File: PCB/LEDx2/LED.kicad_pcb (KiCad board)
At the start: 2 copper layers, 70 x 70 mm, 32 parts, among them J1 Reset, J2 Wago, J3 TC2030-USB-NL-DS, J4 Wago, J5 USB-C-Socket-H, J6 Wago, J7 Wago, U6 ESP32-S3-MINI-1, U7 MD8942

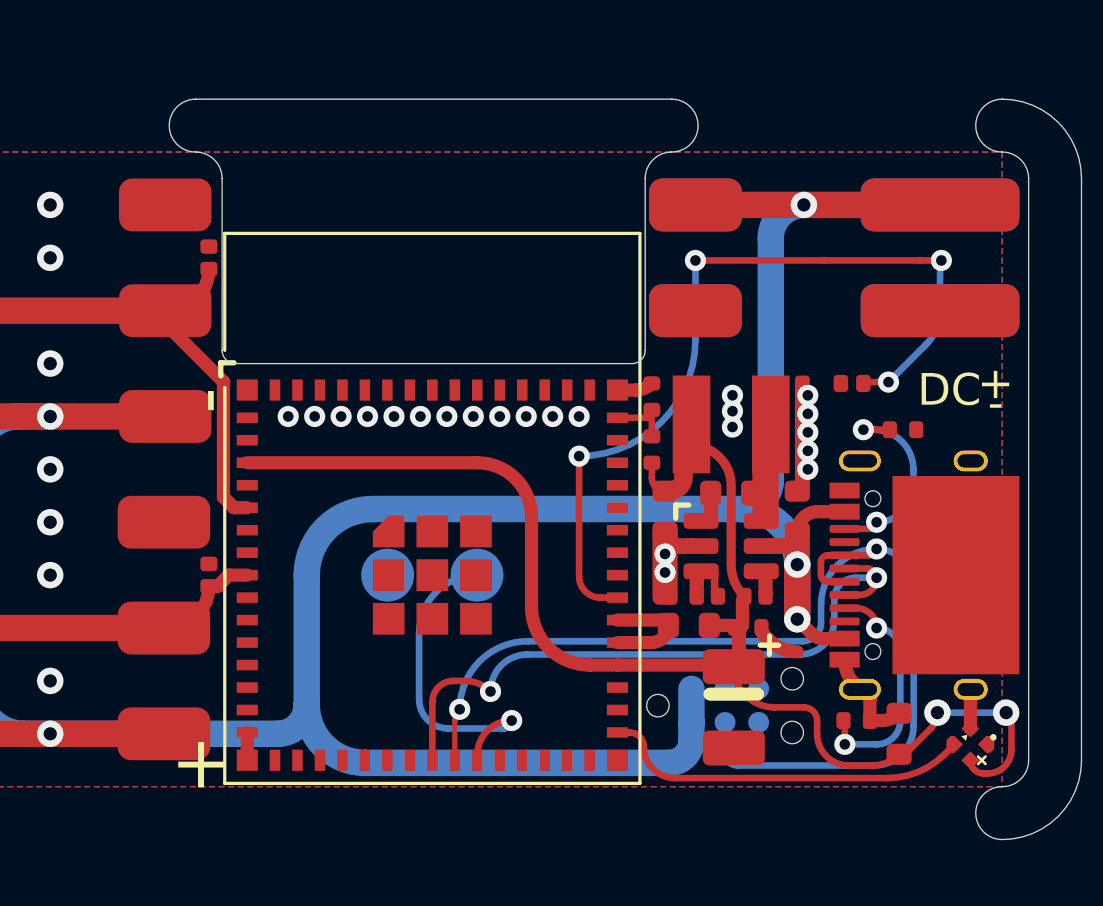
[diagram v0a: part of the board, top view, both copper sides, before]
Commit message: Tidy silkscreen
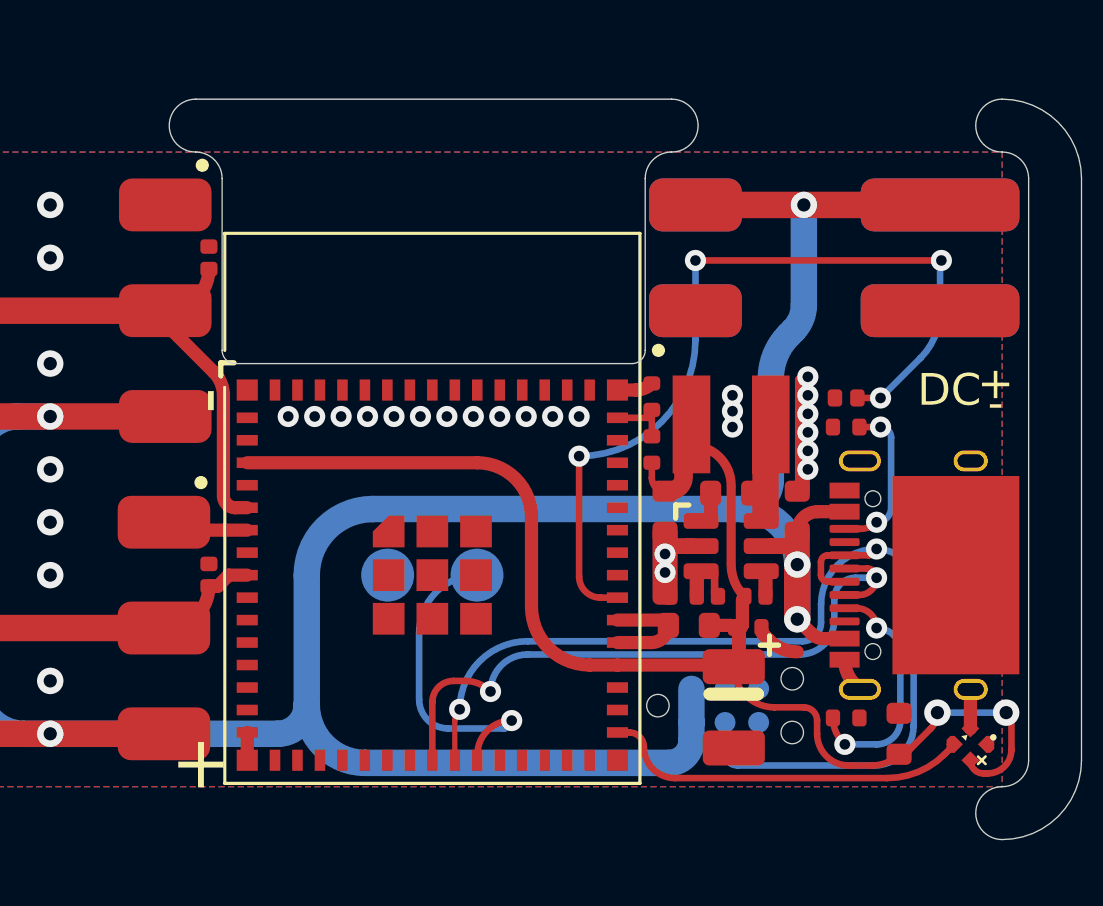
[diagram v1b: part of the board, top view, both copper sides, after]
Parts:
- moved R6 2.15 mm to (114.1, 96.4), turned to 0 degrees
- moved D4 0.59 mm to (114.1, 95.3)
- moved R5 0.41 mm to (114.1, 107.4)
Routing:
- net Net-(J5-CC2): track 7.77 -> 6.18 mm
- net BTN: track 31.9 -> 32.4 mm
- net GND: track 14.0 -> 14.3 mm, vias 29 -> 30

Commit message: SS change
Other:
- board text added: "Made in China for HomeIsWhereTheSmartIs"
- board text added: "www.hiwtsi.uk"
- board text removed: "Made in China for Andrews & Arnold Ltd"
- board text removed: "led.revk.uk"

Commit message: Tidy
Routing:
- net GND: track 14.3 -> 42.1 mm
- net LED2: vias 0 -> 1
- net LED1: vias 0 -> 1

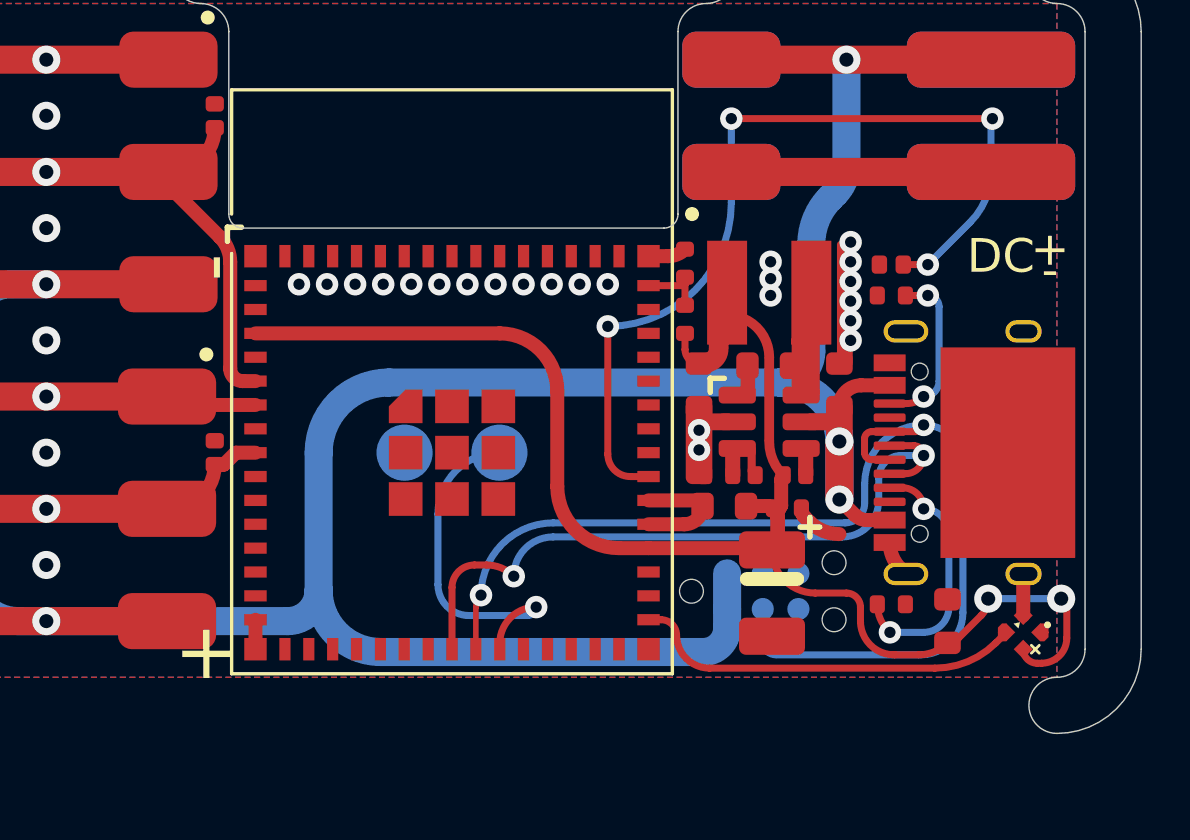
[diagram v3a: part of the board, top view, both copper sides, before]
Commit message: Clean up GND GPIOs
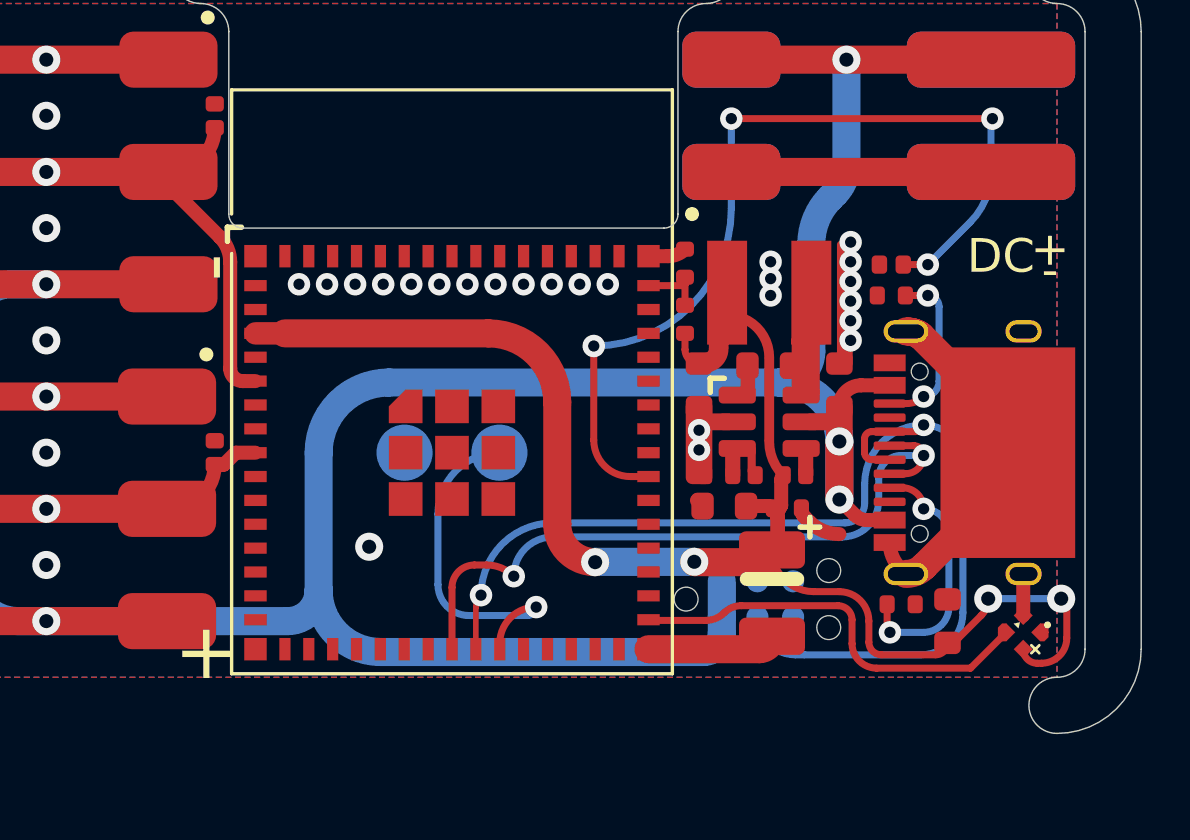
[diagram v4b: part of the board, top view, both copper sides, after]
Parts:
- moved R5 0.35 mm to (114.5, 107.4)
- moved J3 0.34 mm to (109.3, 107.2)
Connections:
- U6 pad 10: GND -> unconnected-(U6-GPIO6-Pad10)
- U6 pad 11: GND -> unconnected-(U6-GPIO7-Pad11)
- U6 pad 12: GND -> unconnected-(U6-GPIO8-Pad12)
- U6 pad 13: GND -> unconnected-(U6-GPIO9-Pad13)
- U6 pad 14: GND -> unconnected-(U6-GPIO10-Pad14)
- U6 pad 15: GND -> unconnected-(U6-GPIO11-Pad15)
- U6 pad 32: GND -> unconnected-(U6-GPIO36-Pad32)
- U6 pad 33: GND -> unconnected-(U6-GPIO37-Pad33)
- U6 pad 34: +3V3 -> unconnected-(U6-GPIO38-Pad34)
- U6 pad 35: GND -> unconnected-(U6-GPIO39-Pad35)
- U6 pad 36: GND -> unconnected-(U6-GPIO40-Pad36)
- U6 pad 38: GND -> unconnected-(U6-GPIO42-Pad38)
- U6 pad 44: GND -> unconnected-(U6-GPIO46-Pad44)
- U6 pad 6: GND -> unconnected-(U6-GPIO2-Pad6)
- U6 pad 9: GND -> unconnected-(U6-GPIO5-Pad9)
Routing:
- net GND: track 42.1 -> 50.6 mm, vias 30 -> 31
- net +3V3: track 47.3 -> 49.1 mm, vias 2 -> 4
- net BLINK: track 14.0 -> 15.0 mm
- net BTN: track 32.4 -> 32.9 mm
- net D+: track 41.8 -> 41.3 mm

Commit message: BOM fix
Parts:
- C10: value 10uF 50V -> 10uF 35V

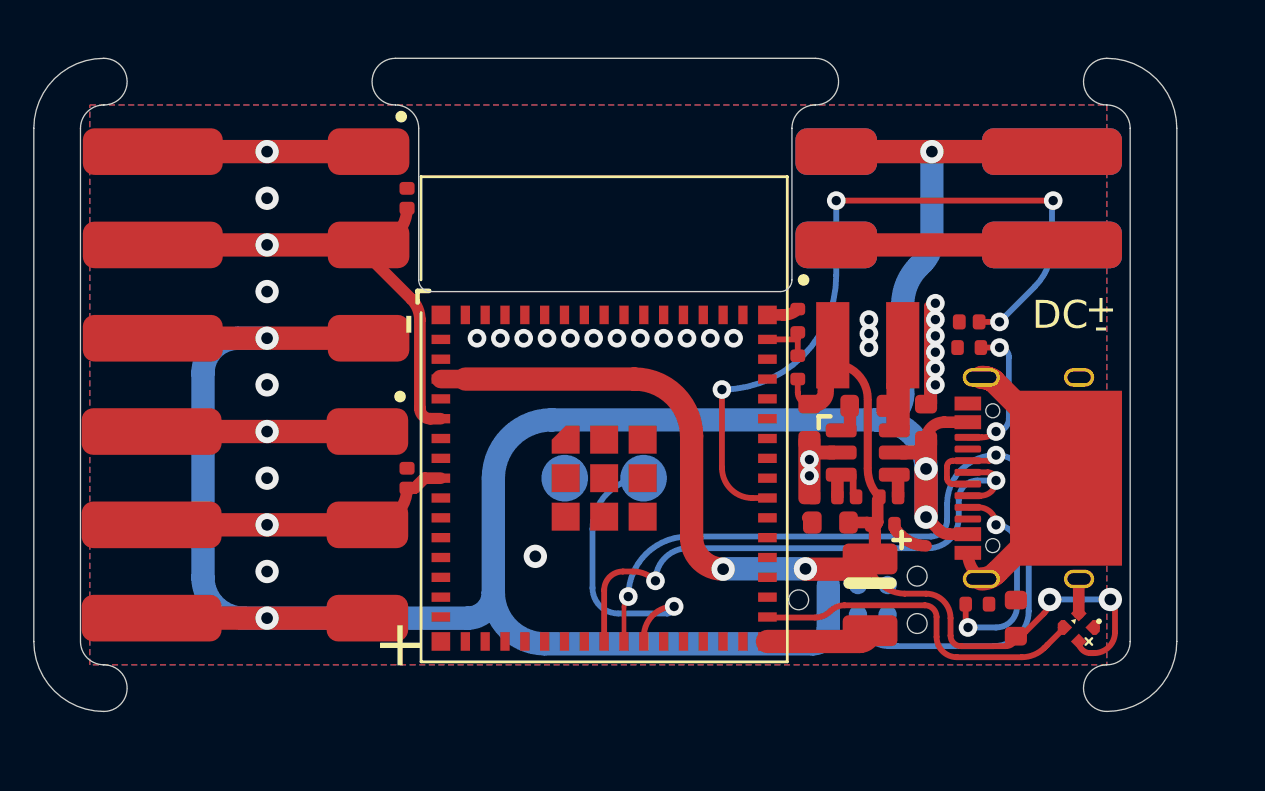
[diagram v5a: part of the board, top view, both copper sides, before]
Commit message: Mic on 2 LED module
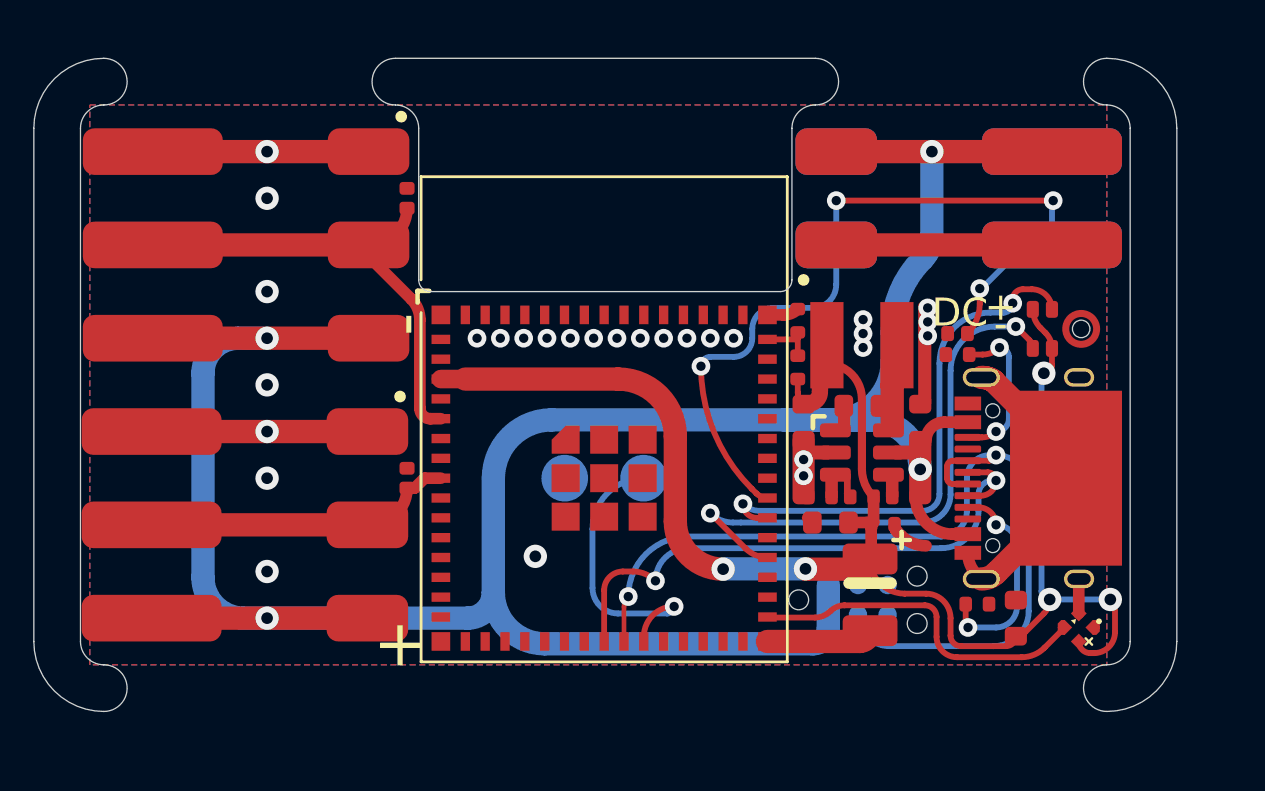
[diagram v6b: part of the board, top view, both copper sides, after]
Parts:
- added T1: T3902_MEMS_Mic, RevK:T3902_MEMS_Mic, F.Cu at (118.2, 95.6)
- moved D4 0.71 mm to (113.6, 95.8)
- moved R6 0.58 mm to (113.6, 96.7)
- moved C12 0.25 mm to (109.5, 98.9)
- moved L2 0.25 mm to (109.5, 96.3)
- moved R14 0.25 mm to (107.7, 102.8)
- moved R15 0.25 mm to (111.3, 102.8)
- moved R4 0.25 mm to (109.5, 102.8)
- moved U7 0.25 mm to (109.5, 100.9)
- turned C1 to 90 degrees
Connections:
- U6 pad 34: unconnected-(U6-GPIO38-Pad34) -> DATA
- U6 pad 36: unconnected-(U6-GPIO40-Pad36) -> CLK
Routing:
- net DATA: track 0.00 -> 24.5 mm, vias 0 -> 2
- net CLK: track 0.00 -> 22.9 mm, vias 0 -> 2
- net +3V3: track 49.1 -> 60.2 mm, vias 4 -> 5
- net GND: track 50.6 -> 46.9 mm, vias 31 -> 28
- net DC: track 118.4 -> 119.1 mm, vias 5 -> 4
- net Net-(J5-CC2): track 6.18 -> 6.75 mm
- net LED2: vias 1 -> 0
- net LED1: vias 1 -> 0
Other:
- board text added: "C40D38"

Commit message: Tweak - add slot
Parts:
- moved C10 0.25 mm to (112.0, 99.6)
- moved C11 0.25 mm to (107.0, 99.6)
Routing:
- net BTN: track 33.1 -> 33.7 mm
- net DC: track 119.1 -> 119.5 mm, vias 4 -> 5
- net GND: vias 28 -> 30

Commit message: New image files
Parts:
- removed REF**: Shadow, RevK:Shadow
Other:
- copper layers 2 -> 4
